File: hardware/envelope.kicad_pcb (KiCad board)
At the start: 4 copper layers, 412.2 x 132 mm, 64 parts, among them J1 Barrel_Jack_Switch_MountingPin, J2 AudioJack3_Switch, J3 AudioJack3_Switch, SW1 SW_DPDT_x2, SW2 SW_SPDT, U1 4066, U2 4069, U3 4069, U4 4510, U5 CD4052B

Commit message: fix power bug
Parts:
- removed G***: LOGO, LOGO
- removed TP11, TP12, TP13, TP21, TP22, TP23, TP31, TP32, TP33: TestPoint, guitar_stuff:poti_hack
- removed U4: 4510, Package_SO:SOIC-16_3.9x9.9mm_P1.27mm
- removed U5: CD4052B, Package_SO:SOIC-16_3.9x9.9mm_P1.27mm
- added ?: LOGO, LOGO, F.Cu at (114.9, 89.5)
- added C4: 100n, Capacitor_SMD:C_0603_1608Metric_Pad1.08x0.95mm_HandSolder, F.Cu at (136.3, 94.6)
- added C5: 100n, Capacitor_SMD:C_0603_1608Metric_Pad1.08x0.95mm_HandSolder, F.Cu at (159.1, 55.1)
- added C7: 100n, Capacitor_SMD:C_0603_1608Metric_Pad1.08x0.95mm_HandSolder, F.Cu at (160.5, 93.2)
- added D1: D_Schottky, Diode_THT:D_A-405_P7.62mm_Horizontal, F.Cu at (183.5, 73.7)
- C9: renamed from C6; moved to F.Cu
- J2, J3: footprint Connector_Audio:jack_raspi_6.3mmjack -> guitar_stuff:newJack
- R10, R16, R5, RV1, RV2, RV3: moved to B.Cu
- R17, R23, R26: moved to F.Cu
- RV4: footprint Potentiometer_THT:Potentiometer_TT_P0915N -> guitar_stuff:alpha_poti
- moved RV1 96.0 mm to (123.0, 57.0), turned to 90 degrees
- moved RV3 93.4 mm to (163.0, 31.6), turned to -90 degrees
- moved C6 92.5 mm to (170.3, 59.9), turned to 90 degrees
- moved D3 89.1 mm to (142.1, 65.3), turned to 0 degrees
- moved R12 84.5 mm to (172.9, 59.9), turned to 90 degrees
- moved R25 83.7 mm to (169.0, 51.3), turned to 180 degrees
- moved R13 82.5 mm to (163.5, 59.7)
- moved R7 82.3 mm to (142.3, 92.9)
- moved J2 81.7 mm to (121.0, 115.1), turned to 180 degrees
- moved R22 81.4 mm to (165.0, 49.3), turned to 0 degrees
- moved D2 81.3 mm to (149.7, 62.3), turned to 180 degrees
- moved R20 80.0 mm to (165.0, 51.3), turned to 180 degrees
- moved C14 79.4 mm to (172.5, 50.3), turned to 90 degrees
- moved U1 76.0 mm to (168.1, 89.6), turned to 180 degrees
- moved C2 75.0 mm to (137.1, 105.8)
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- renumbered C7 to C10, C8 to C11, C9 to C12, C10 to C13, C11 to C14, C4 to C6, C5 to C8, D1 to D2, D2 to D3
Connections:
- J1 pad 2: Net-(J1-Pad2) -> Net-(D1-Pad2)
- J1 pad 3: Net-(J1-Pad2) -> unconnected-(J1-Pad3)
- J2 pad R: unconnected-(J2-PadR) -> GND
- J2 pad S: Net-(J2-PadS) -> GND
- J2 pad T: unconnected-(J2-PadT) -> Net-(J2-PadT)
- J2 pad TN: GND -> Net-(J2-PadT)
- J3 pad R: unconnected-(J3-PadR) -> GND
- J3 pad S: Net-(J3-PadS) -> GND
- J3 pad T: unconnected-(J3-PadT) -> Net-(J3-PadT)
- J3 pad TN: GND -> Net-(J3-PadT)
- R5 pad 2: Net-(J1-Pad2) -> Net-(D1-Pad1)
- SW1 pad 2: Net-(J2-PadS) -> Net-(J2-PadT)
- SW1 pad 5: Net-(J3-PadS) -> Net-(J3-PadT)
- U2 pad 14: GND -> VS
- U2 pad 7: VS -> GND
- U3 pad 14: GND -> VS
- U3 pad 7: VS -> GND
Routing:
- net Net-(R15-Pad2): track 0.00 -> 44.0 mm, vias 0 -> 1
- net TG: track 0.00 -> 38.4 mm
- net Net-(J2-PadT): track 0.00 -> 37.9 mm
- net Net-(J3-PadT): track 0.00 -> 36.7 mm
- net Net-(C14-Pad1): track 0.00 -> 36.4 mm
- net Net-(R10-Pad1): track 0.00 -> 32.7 mm
- net VS: track 0.00 -> 28.1 mm, vias 0 -> 7
- net Net-(C9-Pad1): track 0.00 -> 26.1 mm
- net Net-(C11-Pad2): track 0.00 -> 24.9 mm, vias 0 -> 1
- net Net-(C11-Pad1): track 0.00 -> 23.2 mm
- net Net-(R22-Pad1): track 0.00 -> 23.1 mm
- net Net-(C8-Pad1): track 0.00 -> 22.4 mm
- net Net-(R27-Pad2): track 0.00 -> 21.8 mm, vias 0 -> 1
- net Net-(R13-Pad1): track 0.00 -> 20.6 mm
- net Net-(C14-Pad2): track 0.00 -> 20.5 mm
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- added copper zone on In2.Cu, net GND
- added copper zone on In1.Cu, net VS
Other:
- board size 412.2 x 132 mm -> 86 x 99 mm
- board text added: "Attack"
- board text added: "BYP"
- board text added: "Env"
- board text added: "FXIN"
- board text added: "FXOUT"
- board text added: "IN"
- board text added: "Man"
- board text added: "OUT"
- board text added: "Out"
- board text added: "Pot Manual Filter"
- board text added: "Release"
- board text added: "Threshold"

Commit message: pre via stitch
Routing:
- added copper zone on B.Cu, net GND
- added copper zone on F.Cu, net GND
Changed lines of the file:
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@@
     (56 "User.7" user)
     (57 "User.8" user)
-    (58 "User.9" user)
+    (58 "User.9" user "plugins.config")
   )
   (setup
@@
   (segment (start 179.2375 85.5725) (end 183.5 81.31) (width 2) (layer "F.Cu") (net 53))
   (segment (start 179.2375 88) (end 179.2375 85.5725) (width 2) (layer "F.Cu") (net 53))
-  (zone (net 1) (net_name "VS") (layer "In1.Cu") (hatch edge 0.508)
+  (zone (net 2) (net_name "GND") (layers F&B.Cu) (hatch edge 0.508)
     (connect_pads (clearance 0))
     (min_thickness 0.254) (filled_areas_thickness no)
-    (fill yes (thermal_gap 0.508) (thermal_bridge_width 0.508))
+    (fill yes (mode hatch) (thermal_gap 0.508) (thermal_bridge_width 0.508)
+      (hatch_thickness 0.716) (hatch_gap 1.524) (hatch_orientation 45)
+      (hatch_border_algorithm hatch_thickness) (hatch_min_hole_area 0.3))
     (polygon
       (pts
         (xy 186 30)
         (xy 186 80)
-        (xy 186 134.5)
-        (xy 100 134.5)
+        (xy 186 129.8)
+        (xy 100 129.8)
         (xy 100 55)
         (xy 100 30)
@@
     )
   )
-  (zone (net 2) (net_name "GND") (layer "In2.Cu") (hatch edge 0.508)
+  (zone (net 1) (net_name "VS") (layer "In1.Cu") (hatch edge 0.508)
     (connect_pads (clearance 0))
     (min_thickness 0.254) (filled_areas_thickness no)

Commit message: ground plane
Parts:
- moved J3 0.52 mm to (165.5, 98.6)
- moved J2 0.52 mm to (120.5, 115.1)
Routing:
- net Net-(J3-PadT): track 36.7 -> 37.4 mm
- net Net-(J2-PadT): track 37.9 -> 38.7 mm
- net GND: vias 5 -> 64
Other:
- outline, holes or cut-outs redrawn
- board text added: "{ "ViaStitching": "0.1", "stitch_zone_0": { "HSpacing": "5", "VSpacing": "5", "Clearance": "0.0", "Randomize": false } }"

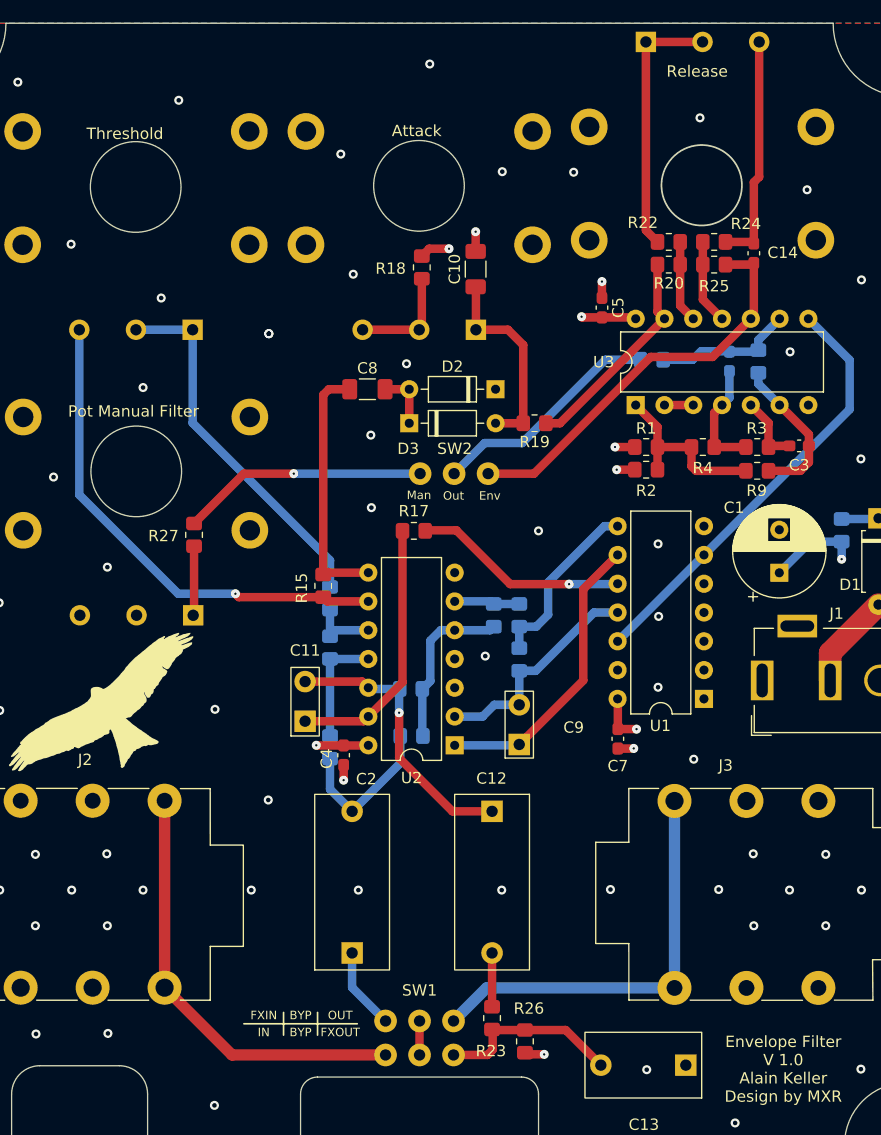
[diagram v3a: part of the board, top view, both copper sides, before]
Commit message: poti footprint updated
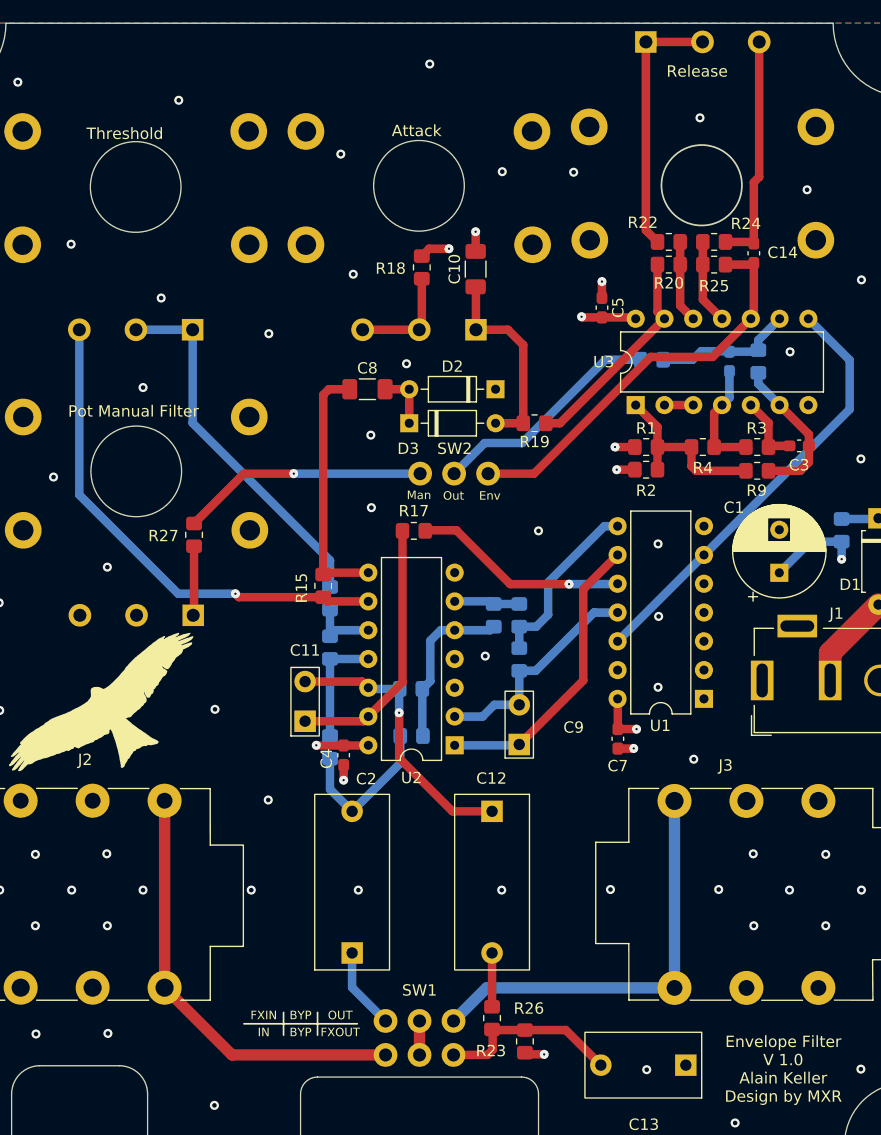
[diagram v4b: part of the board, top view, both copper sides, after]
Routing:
- net Net-(J2-PadT): track 38.7 -> 37.9 mm
- net GND: track 7.61 -> 7.54 mm, vias 64 -> 63
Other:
- board text removed: "{ "ViaStitching": "0.1", "stitch_zone_0": { "HSpacing": "5", "VSpacing": "5", "Clearance": "0.0", "Randomize": false } }"
